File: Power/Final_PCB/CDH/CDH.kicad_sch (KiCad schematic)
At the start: 0 parts

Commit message: CDH Board
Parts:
- added IC1: TEENSY_4.1, TEENSY_4.1:TEENSY41, symbol Teensy:TEENSY_4.1
- added J1: Left_Header, Connector_PinHeader_2.54mm:PinHeader_2x25_P2.54mm_Vertical, symbol Connector_Generic:Conn_02x25_Counter_Clockwise
- added J2: Right_Header, Connector_PinHeader_2.54mm:PinHeader_2x25_P2.54mm_Vertical, symbol Connector_Generic:Conn_02x25_Counter_Clockwise
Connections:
- new net +5V: IC1.55 (VIN_(3.6_TO_5.5_VOLTS))
- new net 14.8V: J1.13 (Pin_13), J1.14 (Pin_14), J1.15 (Pin_15), J1.16 (Pin_16), J2.13 (Pin_13), J2.14 (Pin_14), J2.15 (Pin_15), J2.16 (Pin_16)
- new net 28V: J1.17 (Pin_17), J1.18 (Pin_18), J1.19 (Pin_19), J1.20 (Pin_20), J2.17 (Pin_17), J2.18 (Pin_18), J2.19 (Pin_19), J2.20 (Pin_20)
- new net 3V3: J1.5 (Pin_5), J1.6 (Pin_6), J1.7 (Pin_7), J1.8 (Pin_8), J2.5 (Pin_5), J2.6 (Pin_6), J2.7 (Pin_7), J2.8 (Pin_8)
- new net 5V: J1.10 (Pin_10), J1.11 (Pin_11), J1.12 (Pin_12), J1.9 (Pin_9), J2.10 (Pin_10), J2.11 (Pin_11), J2.12 (Pin_12), J2.9 (Pin_9)
- new net BNO_INT: J1.26 (Pin_26), J2.26 (Pin_26)
- new net BPW34: IC1.22 (A8)
- new net BPW34_OUT: J1.39 (Pin_39), J2.39 (Pin_39)
- new net GND: IC1.45 (GND_1), IC1.48 (GND_2), IC1.49 (GND_3), IC1.69 (GND_4), IC1.70 (GND_5), IC1.71 (GND_6), J1.1 (Pin_1), J1.2 (Pin_2), J1.3 (Pin_3), J1.4 (Pin_4), J1.47 (Pin_47), J1.48 (Pin_48), J1.49 (Pin_49), J1.50 (Pin_50), J2.1 (Pin_1), J2.2 (Pin_2), J2.3 (Pin_3), J2.4 (Pin_4), J2.47 (Pin_47), J2.48 (Pin_48), J2.49 (Pin_49), J2.50 (Pin_50)
- new net GNSS_EN: IC1.25 (A11), J1.42 (Pin_42), J2.42 (Pin_42)
- new net GNSS_FIX: IC1.26 (A12), J1.41 (Pin_41), J2.41 (Pin_41)
- new net GNSS_PPS: IC1.27 (A13), J1.40 (Pin_40), J2.40 (Pin_40)
- new net INA_ALERT: IC1.24 (A10), J1.27 (Pin_27), J2.27 (Pin_27)
- new net L298N_1_ENA: J1.34 (Pin_34), J2.34 (Pin_34)
- new net L298N_1_ENB: J1.33 (Pin_33), J2.33 (Pin_33)
- new net L298N_1_IN1: J1.38 (Pin_38), J2.38 (Pin_38)
- new net L298N_1_IN2: J1.37 (Pin_37), J2.37 (Pin_37)
- new net L298N_1_IN3: J1.36 (Pin_36), J2.36 (Pin_36)
- new net L298N_1_IN4: J1.35 (Pin_35), J2.35 (Pin_35)
- new net L298N_2_ENA: J1.28 (Pin_28), J2.28 (Pin_28)
- new net L298N_2_IN1: J1.32 (Pin_32), J2.32 (Pin_32)
- new net L298N_2_IN2: J1.31 (Pin_31), J2.31 (Pin_31)
- new net L298N_2_IN3: J1.30 (Pin_30), J2.30 (Pin_30)
- new net L298N_2_IN4: J1.29 (Pin_29), J2.29 (Pin_29)
- new net MICROFC: IC1.16 (A2)
- new net RX1: IC1.57 (RX1), J1.44 (Pin_44), J2.44 (Pin_44)
- new net RX2: IC1.7 (RX2), J1.43 (Pin_43), J2.43 (Pin_43)
- new net S1223: IC1.23 (A9)
- new net SCL: IC1.19 (A5), J1.23 (Pin_23), J2.23 (Pin_23)
- new net SDA: IC1.18 (A4), J1.25 (Pin_25), J2.25 (Pin_25)
- new net Status_LED: IC1.15 (A1)
- new net TX1: IC1.1 (TX1), J1.46 (Pin_46), J2.46 (Pin_46)
- new net TX2: IC1.8 (TX2), J1.45 (Pin_45), J2.45 (Pin_45)
- new net VBAT: J1.21 (Pin_21), J1.22 (Pin_22), J2.21 (Pin_21), J2.22 (Pin_22)
- new net XB_RESET: IC1.17 (A3), J1.24 (Pin_24), J2.24 (Pin_24)
- no-connect marks 0 -> 35
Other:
- note added: "Interboard Headers"

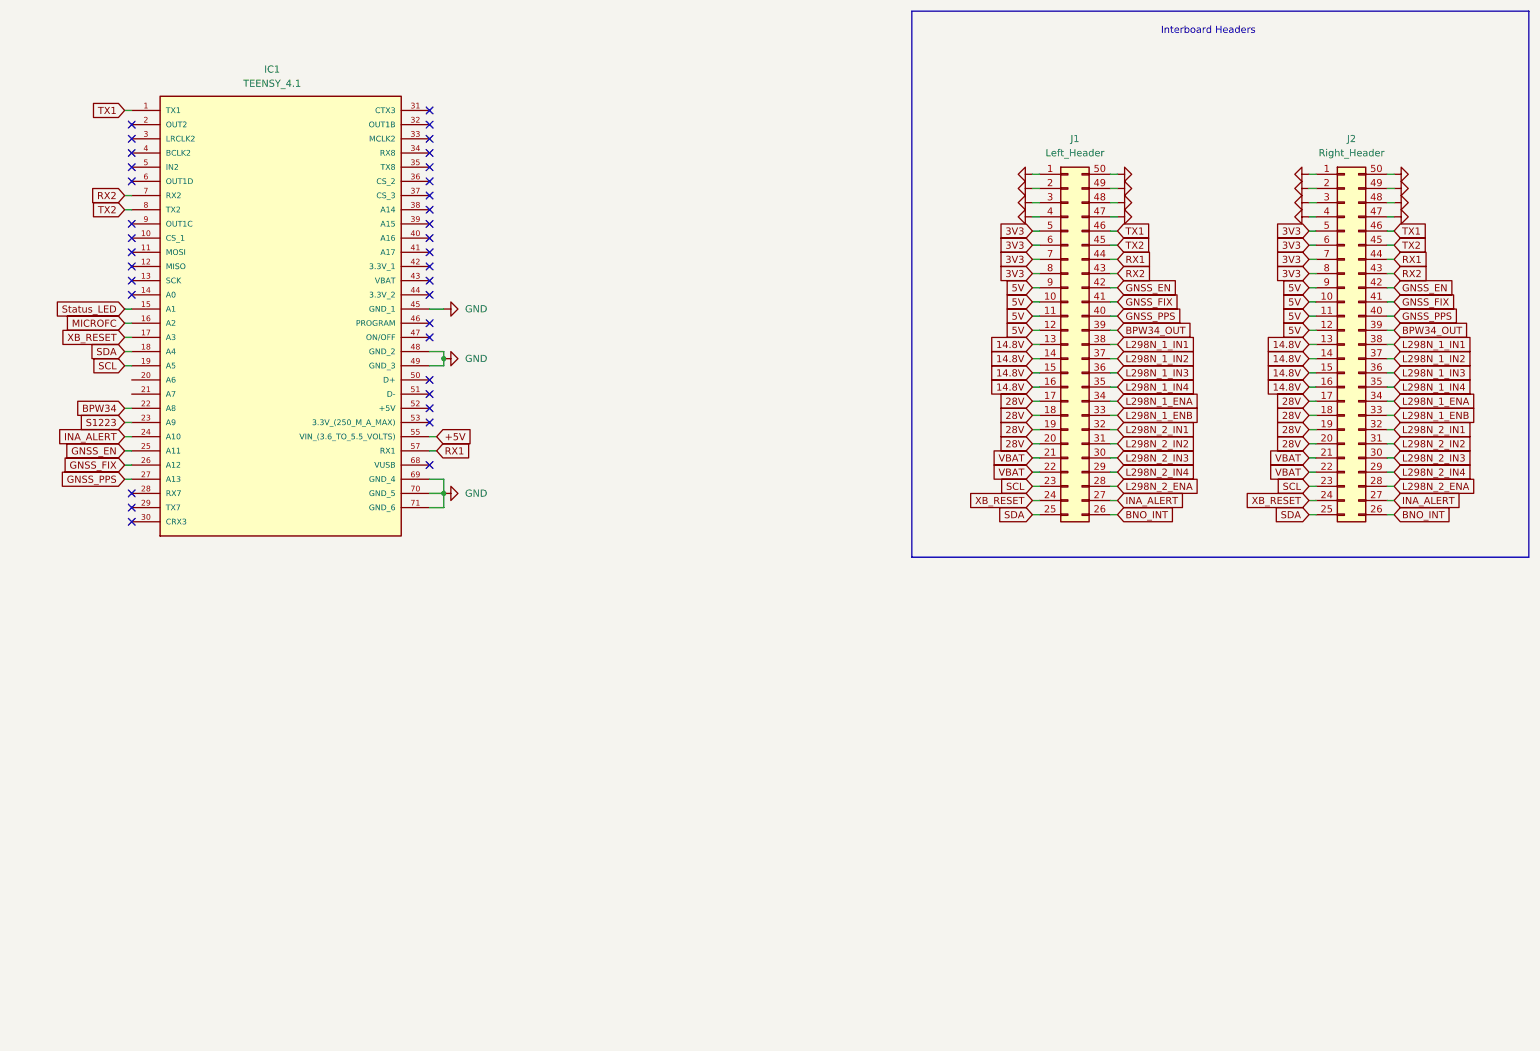
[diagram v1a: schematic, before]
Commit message: CDH board schematic pre motor drivers
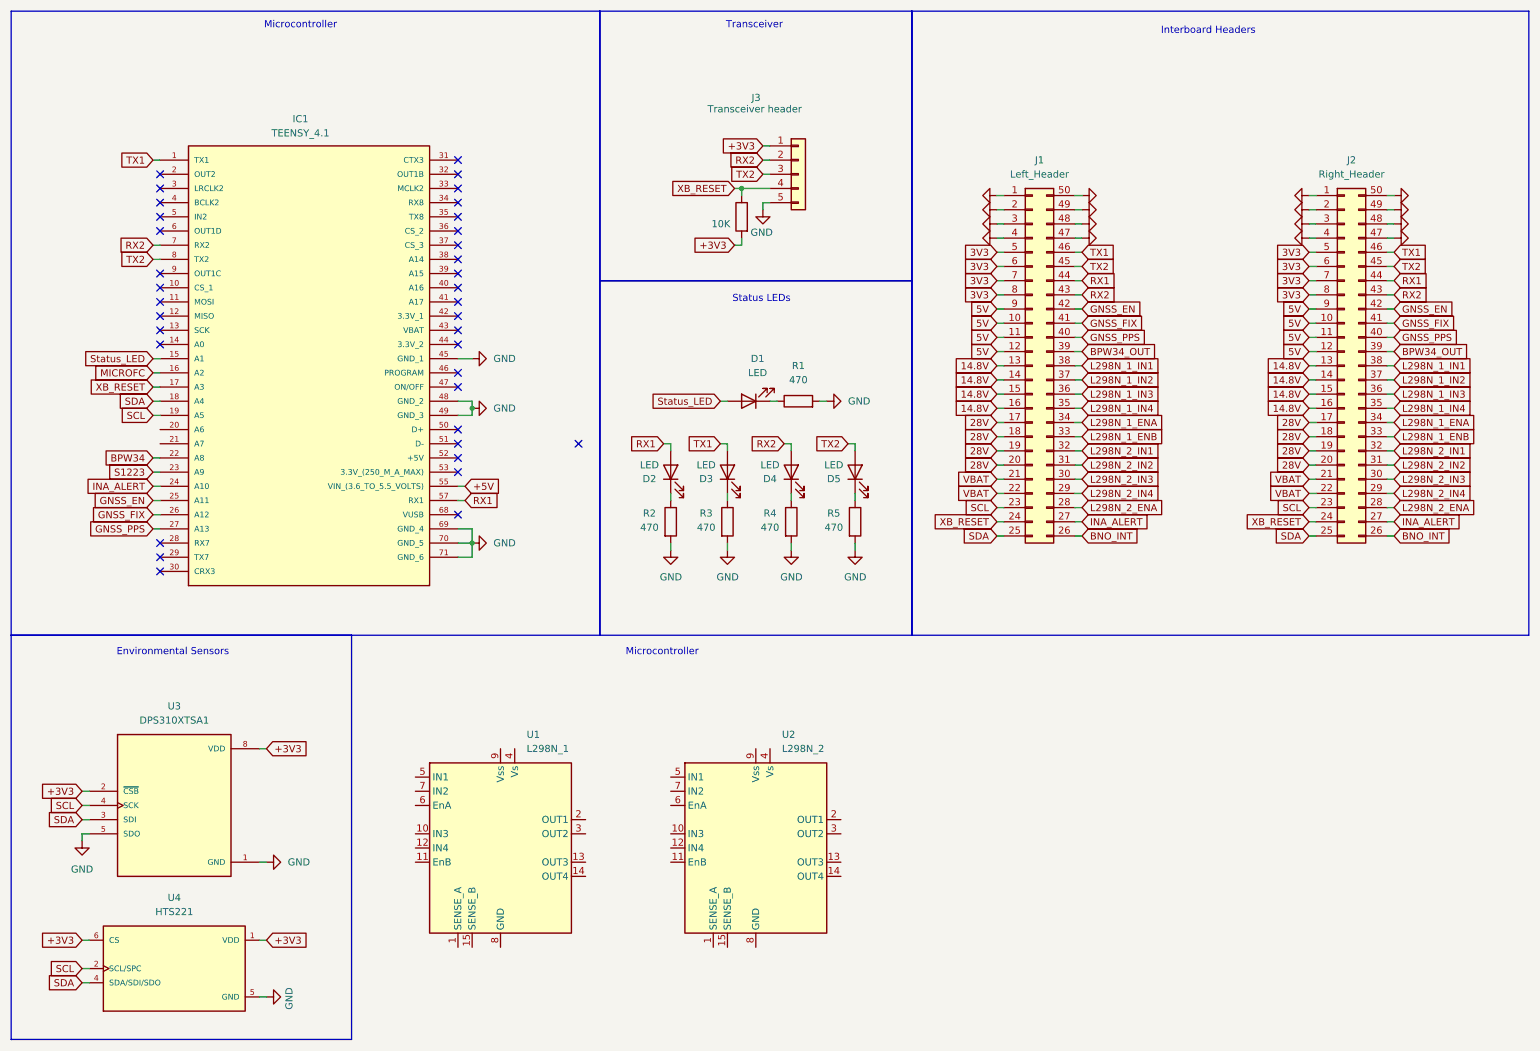
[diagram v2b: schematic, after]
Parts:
- added D1, D2, D3, D4, D5: LED, LED_THT:LED_D3.0mm, symbol Device:LED
- added J3: Transceiver header, Connector_PinHeader_2.54mm:PinHeader_1x05_P2.54mm_Vertical, symbol Connector_Generic:Conn_01x05
- added R1, R2, R3, R4, R5: 470, Resistor_THT:R_Axial_DIN0207_L6.3mm_D2.5mm_P7.62mm_Horizontal, symbol Device:R
- added R10: 10K, Resistor_THT:R_Axial_DIN0207_L6.3mm_D2.5mm_P7.62mm_Horizontal, symbol Device:R
- added U1: L298N_1, Package_TO_SOT_THT:TO-220-15_P2.54x5.08mm_StaggerOdd_Lead4.58mm_Vertical, symbol Driver_Motor:L298N
- added U2: L298N_2, Package_TO_SOT_THT:TO-220-15_P2.54x5.08mm_StaggerOdd_Lead4.58mm_Vertical, symbol Driver_Motor:L298N
- added U3: DPS310XTSA1, DPS310_Breakout:DPS310_Breakout, symbol DPS310_Breakout:DPS310XTSA1
- added U4: HTS221, HTS221_Breakout:HTS221_Breakout, symbol HTS221:HTS221
- IC1: footprint TEENSY_4.1:TEENSY41 -> TEENSY:TEENSY41
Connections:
- net GND: now also J3.5 (Pin_5), R1.2, R2.2, R3.2, R4.2, R5.2, U3.1 (GND), U3.5 (SDO), U4.5 (GND)
- net RX1: now also D2.2 (A)
- net RX2: now also D4.2 (A), J3.2 (Pin_2)
- net SCL: now also U3.4 (SCK), U4.2 (SCL/SPC)
- net SDA: now also U3.3 (SDI), U4.4 (SDA/SDI/SDO)
- net Status_LED: now also D1.2 (A)
- net TX1: now also D3.2 (A)
- net TX2: now also D5.2 (A), J3.3 (Pin_3)
- net XB_RESET: now also J3.4 (Pin_4), R10.1
- new net: D1.1 (K), R1.1
- new net: D2.1 (K), R2.1
- new net: D3.1 (K), R3.1
- new net: D4.1 (K), R4.1
- new net: D5.1 (K), R5.1
- new net +3V3: J3.1 (Pin_1), R10.2, U3.2 (~{CSB}), U3.8 (VDD), U4.1 (VDD), U4.6 (CS)
- no-connect marks 35 -> 36
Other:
- note added: "Environmental Sensors"
- note added: "Microcontroller"
- note added: "Status LEDs"
- note added: "Transceiver"
- moved on the sheet: IC1, J1, J2

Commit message: Fixed EPS board to have 12V instead of 28V rail
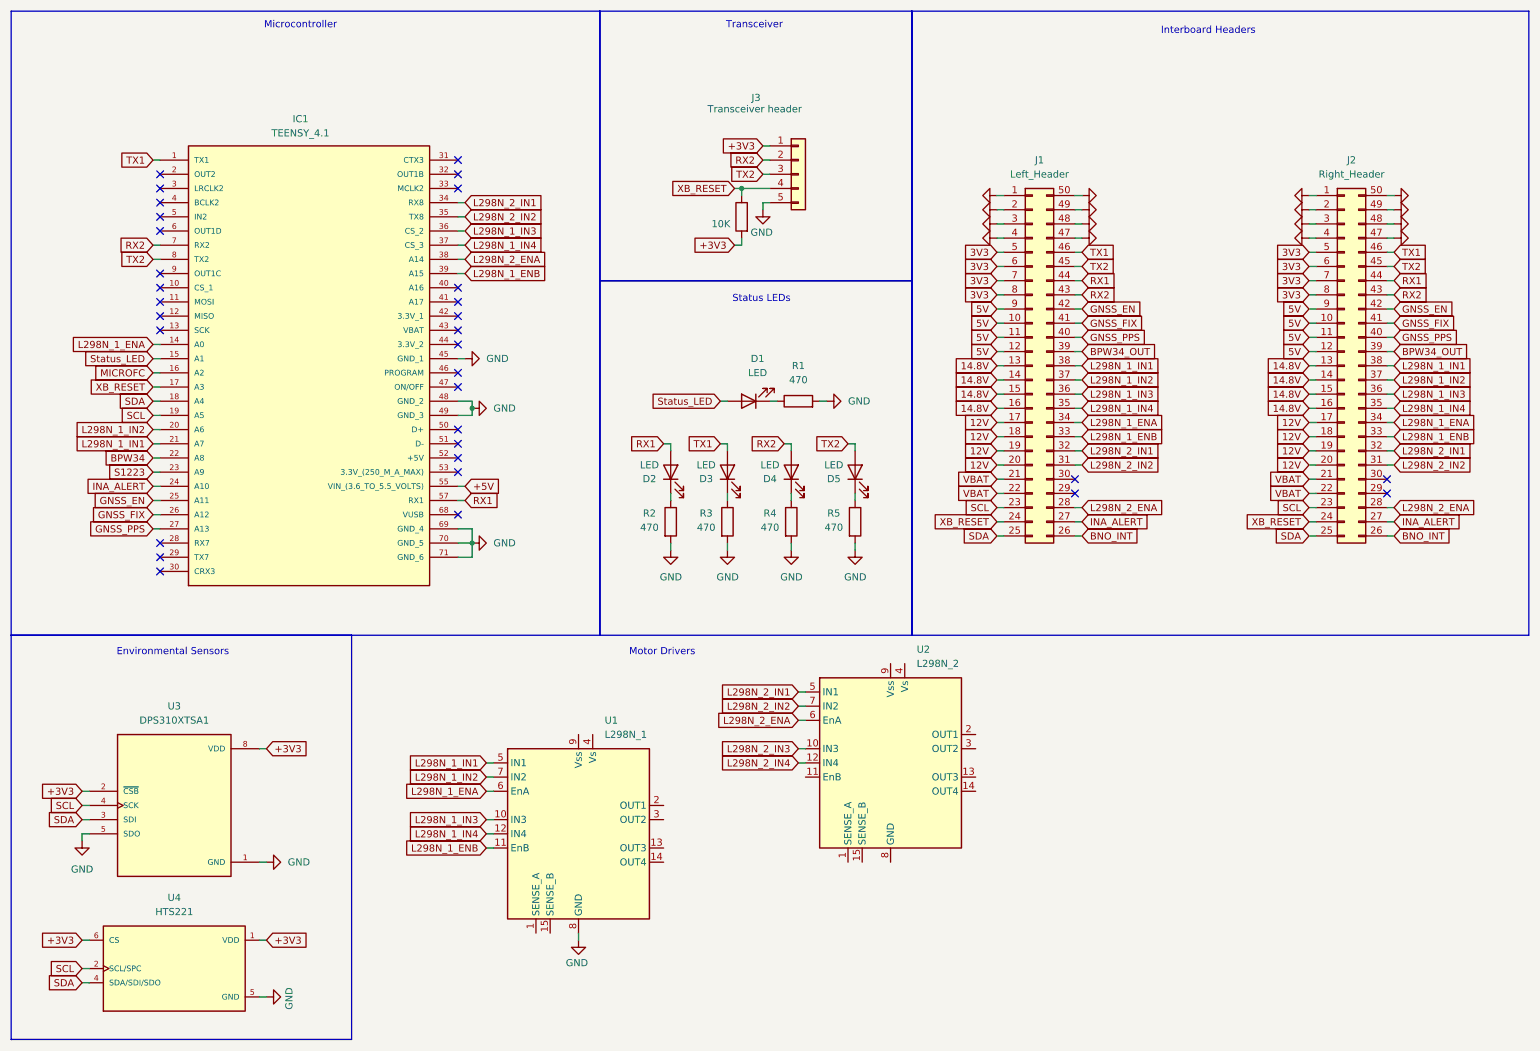
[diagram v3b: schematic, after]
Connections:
- net GND: now also U1.8 (GND)
- net L298N_1_ENA: now also IC1.14 (A0), U1.6 (EnA)
- net L298N_1_ENB: now also IC1.39 (A15), U1.11 (EnB)
- net L298N_1_IN1: now also IC1.21 (A7), U1.5 (IN1)
- net L298N_1_IN2: now also IC1.20 (A6), U1.7 (IN2)
- net L298N_1_IN3: now also IC1.36 (CS_2), U1.10 (IN3)
- net L298N_1_IN4: now also IC1.37 (CS_3), U1.12 (IN4)
- net L298N_2_ENA: now also IC1.38 (A14), U2.6 (EnA)
- net L298N_2_IN1: now also IC1.34 (RX8), U2.5 (IN1)
- net L298N_2_IN2: now also IC1.35 (TX8), U2.7 (IN2)
- net L298N_2_IN3: now also U2.10 (IN3); no longer J1.30 (Pin_30), J2.30 (Pin_30)
- net L298N_2_IN4: now also U2.12 (IN4); no longer J1.29 (Pin_29), J2.29 (Pin_29)
- net 28V renamed 12V
- no-connect marks 36 -> 32
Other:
- note added: "Motor Drivers"
- company: (none) -> Project SunSat
- title: (none) -> HYPERYIONyX - CDH Board
- moved on the sheet: U1, U2

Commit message: Transitioned to ADCS-free version for worst case manufacturing scenario
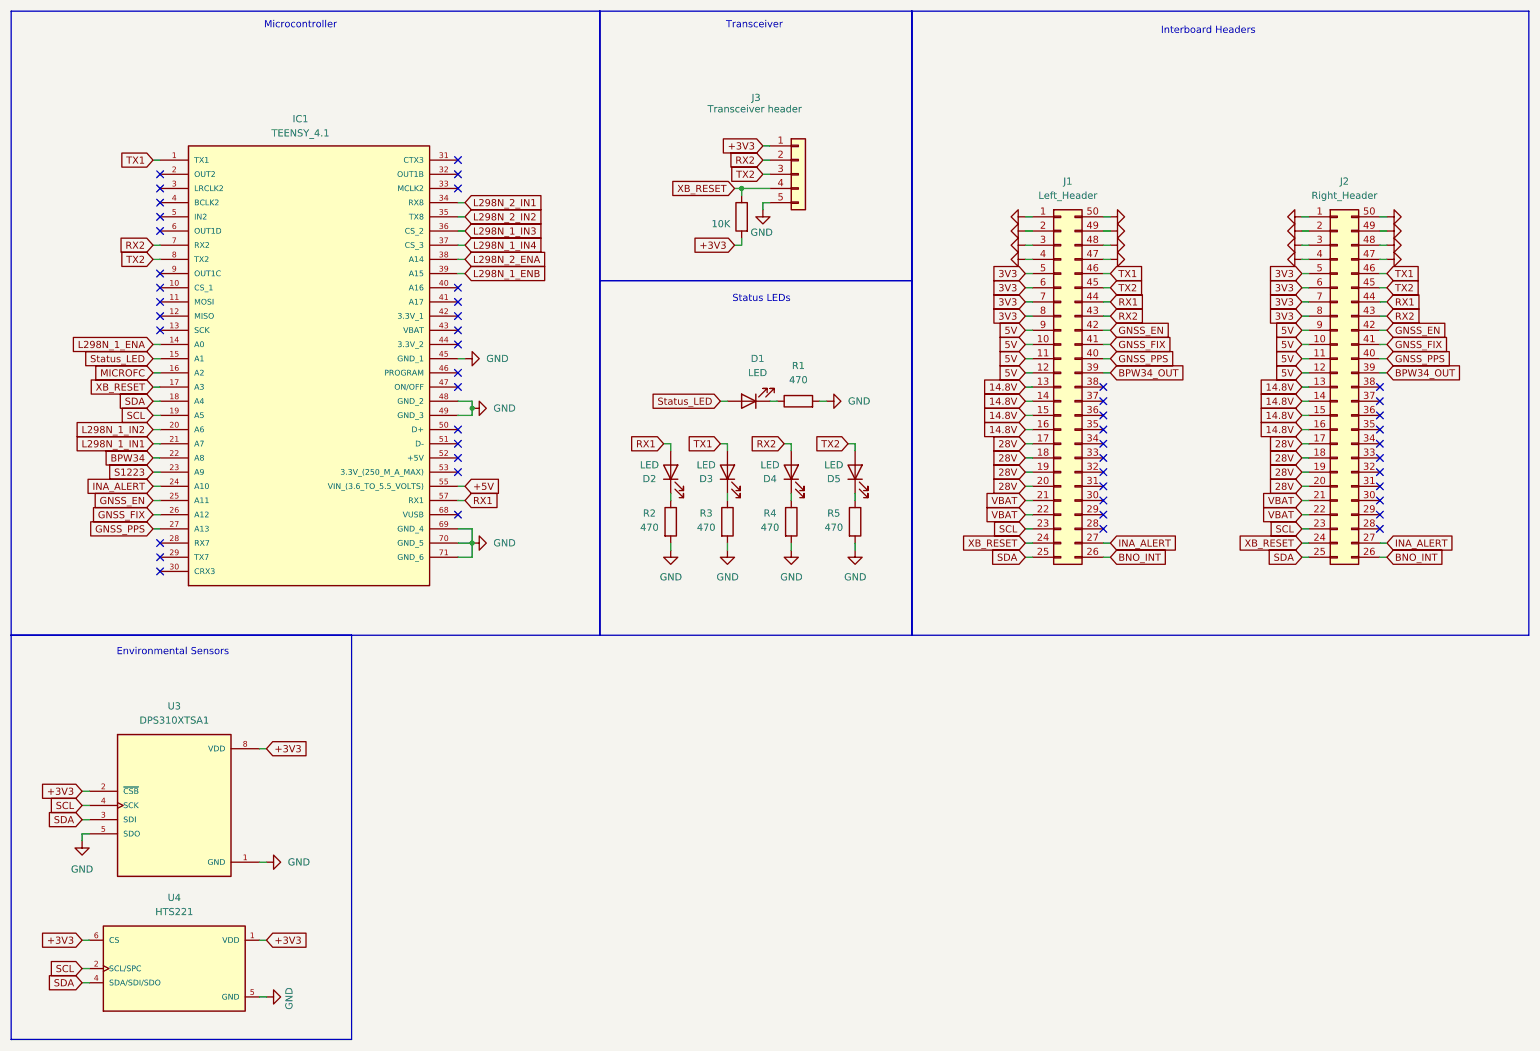
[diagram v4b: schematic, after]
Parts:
- removed U1: L298N_1, Package_TO_SOT_THT:TO-220-15_P2.54x5.08mm_StaggerOdd_Lead4.58mm_Vertical, symbol Driver_Motor:L298N
- removed U2: L298N_2, Package_TO_SOT_THT:TO-220-15_P2.54x5.08mm_StaggerOdd_Lead4.58mm_Vertical, symbol Driver_Motor:L298N
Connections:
- net L298N_1_ENA: no longer J1.34 (Pin_34), J2.34 (Pin_34)
- net L298N_1_ENB: no longer J1.33 (Pin_33), J2.33 (Pin_33)
- net L298N_1_IN1: no longer J1.38 (Pin_38), J2.38 (Pin_38)
- net L298N_1_IN2: no longer J1.37 (Pin_37), J2.37 (Pin_37)
- net L298N_1_IN3: no longer J1.36 (Pin_36), J2.36 (Pin_36)
- net L298N_1_IN4: no longer J1.35 (Pin_35), J2.35 (Pin_35)
- net L298N_2_ENA: no longer J1.28 (Pin_28), J2.28 (Pin_28)
- net L298N_2_IN1: no longer J1.32 (Pin_32), J2.32 (Pin_32)
- net L298N_2_IN2: no longer J1.31 (Pin_31), J2.31 (Pin_31)
- net 12V renamed 28V
- no-connect marks 32 -> 50
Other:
- note removed: "Motor Drivers"

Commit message: Completed CDH Board
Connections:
- net L298N_1_ENA: no longer names the net of IC1.14 (A0)
- net L298N_1_ENB: no longer names the net of IC1.39 (A15)
- net L298N_1_IN1: no longer names the net of IC1.21 (A7)
- net L298N_1_IN2: no longer names the net of IC1.20 (A6)
- net L298N_1_IN3: no longer names the net of IC1.36 (CS_2)
- net L298N_1_IN4: no longer names the net of IC1.37 (CS_3)
- net L298N_2_ENA: no longer names the net of IC1.38 (A14)
- net L298N_2_IN1: no longer names the net of IC1.34 (RX8)
- net L298N_2_IN2: no longer names the net of IC1.35 (TX8)
- no-connect marks 50 -> 59

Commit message: Finalising Sensors Schematic
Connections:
- net BNO_INT: now also IC1.2 (OUT2)
- net MICROFC: now also J1.28 (Pin_28), J2.28 (Pin_28)
- net S1223: now also J1.29 (Pin_29), J2.29 (Pin_29)
- net BNO_RST: now reaches J2.30 (Pin_30)
- net BNO_RST: now also IC1.3 (LRCLK2), J1.30 (Pin_30)
- no-connect marks 59 -> 51
